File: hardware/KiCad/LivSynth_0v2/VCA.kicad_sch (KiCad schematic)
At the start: 22 parts, among them J18 Jumper, J6 Jumper, Q5 2N3904, Q6 2N3904, U1 TL074

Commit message: Geographical reannotate
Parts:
- renumbered J6 to J10, Q5 to Q4, Q6 to Q5, R3 to R10, R66 to R26, R37 to R28, R62 to R44, R67 to R45, R65 to R46, R60 to R47, R39 to R56, R63 to R57, R57 to R58, R58 to R59, R20 to R7, R38 to R8, R17 to R9, RV1001 to RV1, RV11 to RV8
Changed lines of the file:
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@@
   (symbol (lib_id "Device:R") (at 132.08 56.515 0) (unit 1)
     (in_bom yes) (on_board yes)
-    (property "Reference" "R17" (id 0) (at 133.985 55.2449 0)
+    (property "Reference" "R9" (id 0) (at 133.985 55.2449 0)
       (effects (font (size 1.27 1.27)) (justify left))
     )
@@
   (symbol (lib_id "Device:R") (at 120.65 109.22 0) (unit 1)
     (in_bom yes) (on_board yes) (fields_autoplaced)
-    (property "Reference" "R37" (id 0) (at 123.19 107.9499 0)
+    (property "Reference" "R28" (id 0) (at 123.19 107.9499 0)
       (effects (font (size 1.27 1.27)) (justify left))
     )
@@
   (symbol (lib_id "Device:R") (at 95.885 87.63 0) (unit 1)
     (in_bom yes) (on_board yes) (fields_autoplaced)
-    (property "Reference" "R38" (id 0) (at 98.425 86.3599 0)
+    (property "Reference" "R8" (id 0) (at 98.425 86.3599 0)
       (effects (font (size 1.27 1.27)) (justify left))
     )
@@
   (symbol (lib_id "Device:R") (at 86.995 147.32 90) (unit 1)
     (in_bom yes) (on_board yes)
-    (property "Reference" "R39" (id 0) (at 86.995 140.97 90))
+    (property "Reference" "R56" (id 0) (at 86.995 140.97 90))
     (property "Value" "100K" (id 1) (at 86.995 143.51 90))
     (property "Footprint" "Resistor_THT:R_Axial_DIN0207_L6.3mm_D2.5mm_P7.62mm_Horizontal" (id 2) (at 86.995 149.098 90)
@@
   (symbol (lib_id "Device:R_Potentiometer_Trim") (at 120.65 50.8 90) (unit 1)
     (in_bom yes) (on_board yes) (fields_autoplaced)
-    (property "Reference" "RV1001" (id 0) (at 120.65 54.864 90))
+    (property "Reference" "RV1" (id 0) (at 120.65 54.864 90))
     (property "Value" "1K" (id 1) (at 120.65 57.404 90))
     (property "Footprint" "SloBlo:Potentiometer_Bourns_3296W_Vertical" (id 2) (at 120.65 50.8 0)
@@
   (symbol (lib_id "Device:R") (at 108.585 56.515 0) (unit 1)
     (in_bom yes) (on_board yes)
-    (property "Reference" "R20" (id 0) (at 110.49 55.2449 0)
+    (property "Reference" "R7" (id 0) (at 110.49 55.2449 0)
       (effects (font (size 1.27 1.27)) (justify left))
     )
@@
   (symbol (lib_id "Device:R") (at 76.835 137.795 0) (unit 1)
     (in_bom yes) (on_board yes) (fields_autoplaced)
-    (property "Reference" "R63" (id 0) (at 79.375 136.5249 0)
+    (property "Reference" "R57" (id 0) (at 79.375 136.5249 0)
       (effects (font (size 1.27 1.27)) (justify left))
     )
@@
   (symbol (lib_id "Device:R") (at 86.995 117.475 90) (unit 1)
     (in_bom yes) (on_board yes) (fields_autoplaced)
-    (property "Reference" "R62" (id 0) (at 86.995 111.125 90))
+    (property "Reference" "R44" (id 0) (at 86.995 111.125 90))
     (property "Value" "100K" (id 1) (at 86.995 113.665 90))
     (property "Footprint" "Resistor_THT:R_Axial_DIN0207_L6.3mm_D2.5mm_P7.62mm_Horizontal" (id 2) (at 86.995 119.253 90)
@@
   (symbol (lib_id "Transistor_BJT:2N3904") (at 106.045 78.105 0) (unit 1)
     (in_bom yes) (on_board yes) (fields_autoplaced)
-    (property "Reference" "Q5" (id 0) (at 111.76 76.8349 0)
+    (property "Reference" "Q4" (id 0) (at 111.76 76.8349 0)
       (effects (font (size 1.27 1.27)) (justify left))
     )
@@
   (symbol (lib_id "Device:R") (at 108.585 133.985 90) (unit 1)
     (in_bom yes) (on_board yes) (fields_autoplaced)
-    (property "Reference" "R58" (id 0) (at 108.585 128.27 90))
+    (property "Reference" "R59" (id 0) (at 108.585 128.27 90))
     (property "Value" "47K" (id 1) (at 108.585 130.81 90))
     (property "Footprint" "Resistor_THT:R_Axial_DIN0207_L6.3mm_D2.5mm_P7.62mm_Horizontal" (id 2) (at 108.585 135.763 90)
@@
   (symbol (lib_id "Connector:Conn_01x02_Male") (at 71.12 73.025 90) (mirror x) (unit 1)
     (in_bom yes) (on_board yes) (fields_autoplaced)
-    (property "Reference" "J6" (id 0) (at 74.93 72.3899 90)
+    (property "Reference" "J10" (id 0) (at 74.93 72.3899 90)
       (effects (font (size 1.27 1.27)) (justify right))
     )
@@
   (symbol (lib_id "Device:R") (at 163.83 63.5 90) (unit 1)
     (in_bom yes) (on_board yes) (fields_autoplaced)
-    (property "Reference" "R67" (id 0) (at 163.83 57.785 90))
+    (property "Reference" "R45" (id 0) (at 163.83 57.785 90))
     (property "Value" "1K" (id 1) (at 163.83 60.325 90))
     (property "Footprint" "Resistor_THT:R_Axial_DIN0207_L6.3mm_D2.5mm_P7.62mm_Horizontal" (id 2) (at 163.83 65.278 90)
@@
   (symbol (lib_id "Device:R") (at 86.995 78.105 90) (unit 1)
     (in_bom yes) (on_board yes) (fields_autoplaced)
-    (property "Reference" "R3" (id 0) (at 86.995 71.755 90))
+    (property "Reference" "R10" (id 0) (at 86.995 71.755 90))
     (property "Value" "100K" (id 1) (at 86.995 74.295 90))
     (property "Footprint" "Resistor_THT:R_Axial_DIN0207_L6.3mm_D2.5mm_P7.62mm_Horizontal" (id 2) (at 86.995 79.883 90)
@@
   (symbol (lib_id "Device:R") (at 163.83 68.58 90) (unit 1)
     (in_bom yes) (on_board yes)
-    (property "Reference" "R65" (id 0) (at 163.83 73.66 90))
+    (property "Reference" "R46" (id 0) (at 163.83 73.66 90))
     (property "Value" "1K" (id 1) (at 163.83 71.12 90))
     (property "Footprint" "Resistor_THT:R_Axial_DIN0207_L6.3mm_D2.5mm_P7.62mm_Horizontal" (id 2) (at 163.83 70.358 90)
@@
   (symbol (lib_id "Device:R_Potentiometer") (at 76.835 147.32 0) (mirror x) (unit 1)
     (in_bom yes) (on_board yes) (fields_autoplaced)
-    (property "Reference" "RV11" (id 0) (at 74.93 146.0499 0)
+    (property "Reference" "RV8" (id 0) (at 74.93 146.0499 0)
       (effects (font (size 1.27 1.27)) (justify right))
     )
@@
   (symbol (lib_id "Transistor_BJT:2N3904") (at 134.62 78.105 0) (mirror y) (unit 1)
     (in_bom yes) (on_board yes) (fields_autoplaced)
-    (property "Reference" "Q6" (id 0) (at 129.54 76.8349 0)
+    (property "Reference" "Q5" (id 0) (at 129.54 76.8349 0)
       (effects (font (size 1.27 1.27)) (justify left))
     )
@@
   (symbol (lib_id "Device:R") (at 189.23 50.8 270) (unit 1)
     (in_bom yes) (on_board yes) (fields_autoplaced)
-    (property "Reference" "R66" (id 0) (at 189.23 45.085 90))
+    (property "Reference" "R26" (id 0) (at 189.23 45.085 90))
     (property "Value" "100K" (id 1) (at 189.23 47.625 90))
     (property "Footprint" "Resistor_THT:R_Axial_DIN0207_L6.3mm_D2.5mm_P7.62mm_Horizontal" (id 2) (at 189.23 49.022 90)
@@
   (symbol (lib_id "Device:R") (at 177.8 74.93 180) (unit 1)
     (in_bom yes) (on_board yes) (fields_autoplaced)
-    (property "Reference" "R60" (id 0) (at 179.705 73.6599 0)
+    (property "Reference" "R47" (id 0) (at 179.705 73.6599 0)
       (effects (font (size 1.27 1.27)) (justify right))
     )
@@
   (symbol (lib_id "Device:R") (at 76.835 157.48 0) (unit 1)
     (in_bom yes) (on_board yes) (fields_autoplaced)
-    (property "Reference" "R57" (id 0) (at 78.74 156.2099 0)
-      (effects (font (size 1.27 1.27)) (justify left))
-    )
+    (property "Reference" "R58" (id 0) (at 78.74 156.2099 0)
+      (effects (font (size 1.27 1.27)) (justify left))
+    )

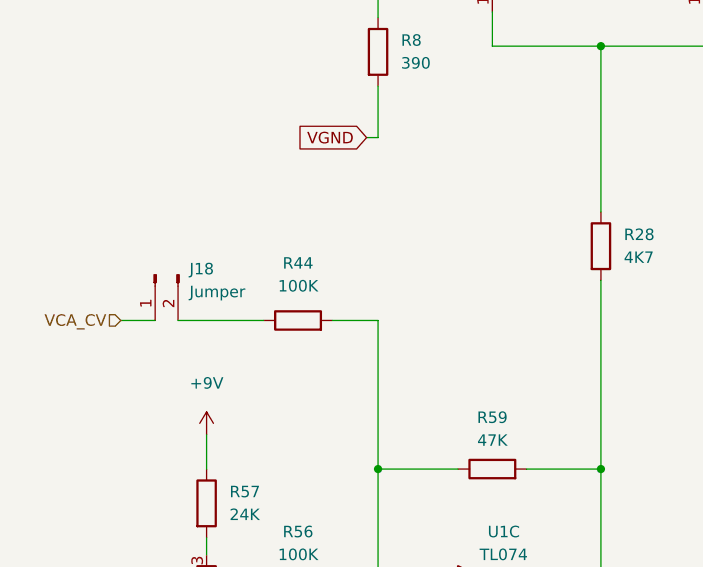
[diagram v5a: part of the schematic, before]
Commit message: Increase loudness
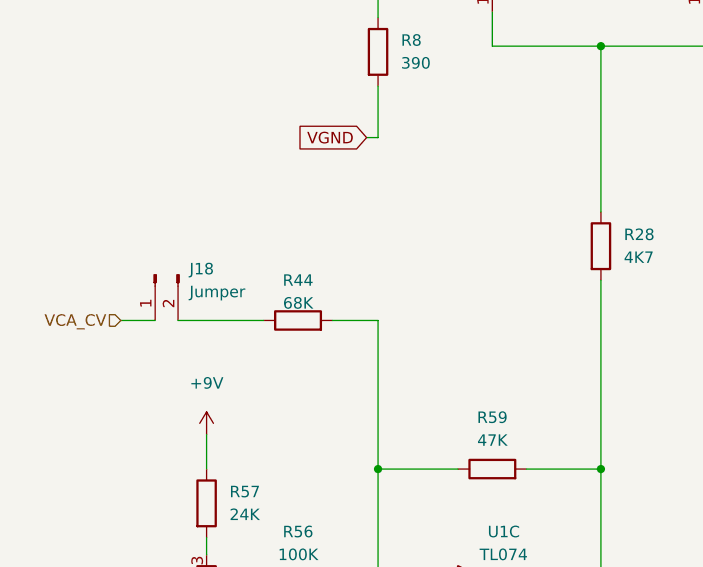
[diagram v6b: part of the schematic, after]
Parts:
- R44: value 100K -> 68K
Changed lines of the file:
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@@
   (symbol (lib_id "Device:R") (at 86.995 117.475 90) (unit 1)
     (in_bom yes) (on_board yes) (dnp no) (fields_autoplaced)
-    (property "Reference" "R44" (at 86.995 111.125 90)
+    (property "Reference" "R44" (at 86.995 113.03 90)
       (effects (font (size 1.27 1.27)))
     )
-    (property "Value" "100K" (at 86.995 113.665 90)
+    (property "Value" "68K" (at 86.995 115.57 90)
       (effects (font (size 1.27 1.27)))
     )
